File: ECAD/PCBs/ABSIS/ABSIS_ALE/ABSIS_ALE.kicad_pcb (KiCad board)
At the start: 2 copper layers, 36 x 51 mm, 16 parts, among them J1 BUS IN, J2 BUS OUT, J3 I/O #1, J4 I/O #2, J5 GND, J6 ACC PWR, U1 MAX487EESA+T

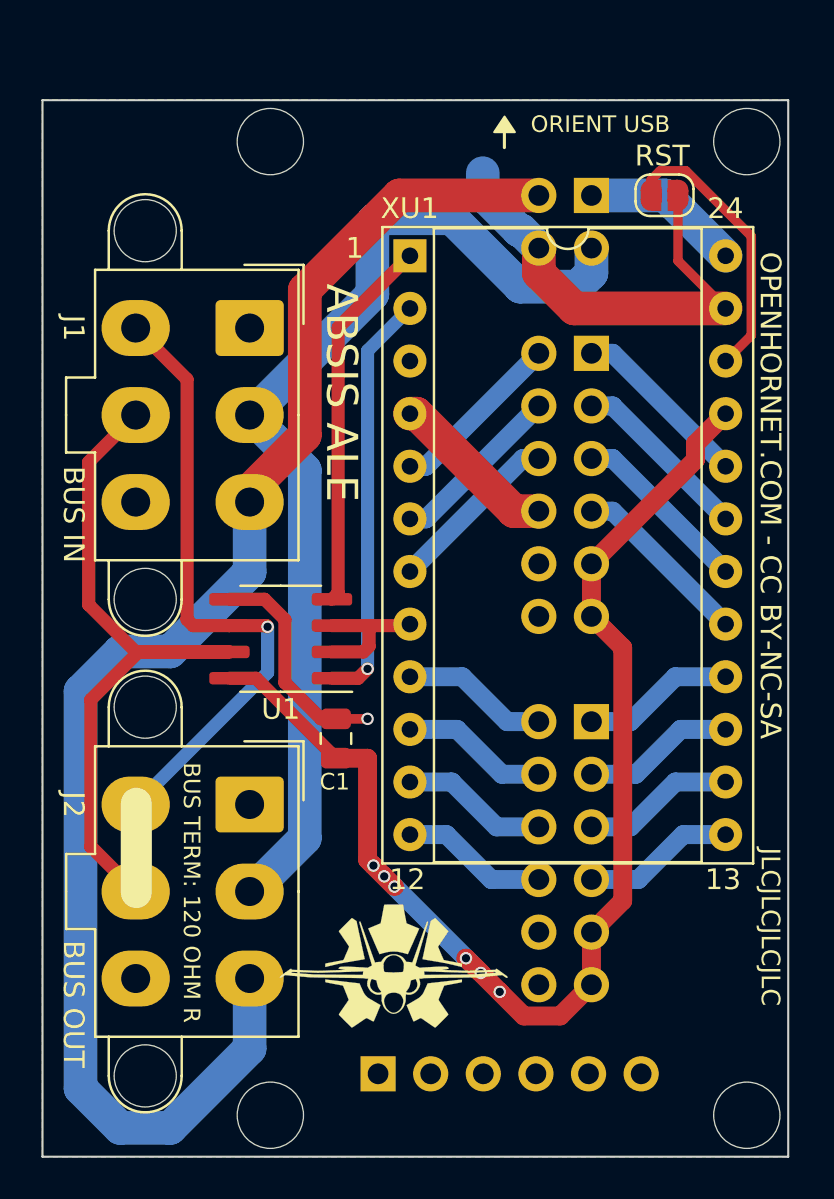
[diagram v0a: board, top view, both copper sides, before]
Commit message: OH Library Update + ABSIS_ALE Final Check
----OH_3DModels Library----
Added: PinHeader_1x06_P2.54mm_Vertical
Added: PinHeader_2x02_P2.54mm_Vertical
Added: PinHeader_2x06_P2.54mm_Vertical
Added: DIP-24_W15.24mm_Socket
Added: C_0805_2012Metric

----OH_Footprints Library----
Added: Molex_Mini-Fit_Jr_5566-06A2_2x03_P4.20mm_Vertical
Added: DIP-24_W15.24mm_Socket
Added: PinHeader_1x06_P2.54mm_Vertical
Added: PinHeader_2x02_P2.54mm_Vertical
Added: PinHeader_2x06_P2.54mm_Vertical
Added: C_0805_2012Metric
Added: SolderJumper-2_P1.3mm_Open_RoundedPad1.0x1.5mm
Added: SOIC-8_3.9x4.9mm_P1.27mm

- Updated ABSIS_ALE PCB with New footprint/Model locations
- Added 4x 3D pictures to Fold (TOP, TOP-ISO, BOT, BOT-ISO)
- Updated STEP File with 3d Models
- Regenerated Manufacturing Files with Updated Part Numbers
- Updated Schematic with correct footprint and model paths.
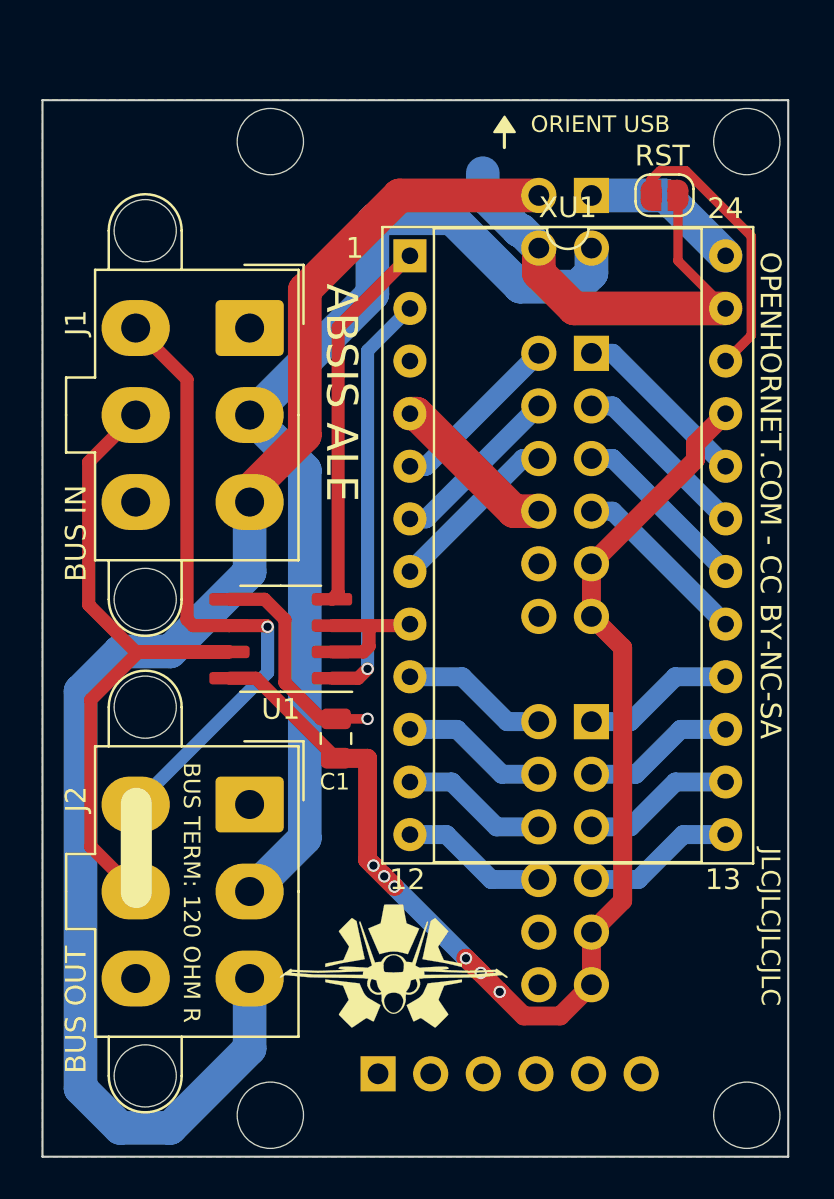
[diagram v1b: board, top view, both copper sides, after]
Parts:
- C1: footprint Capacitor_SMD:C_0805_2012Metric -> OH_Footprints:C_0805_2012Metric
- J1, J2: footprint Connector_Molex:Molex_Mini-Fit_Jr_5566-06A2_2x03_P4.20mm_Vertical -> OH_Footprints:Molex_Mini-Fit_Jr_5566-06A2_2x03_P4.20mm_Vertical
- J3, J4: footprint Connector_PinHeader_2.54mm:PinHeader_2x06_P2.54mm_Vertical -> OH_Footprints:PinHeader_2x06_P2.54mm_Vertical
- J5: footprint Connector_PinHeader_2.54mm:PinHeader_1x06_P2.54mm_Vertical -> OH_Footprints:PinHeader_1x06_P2.54mm_Vertical
- J6: footprint Connector_PinHeader_2.54mm:PinHeader_2x02_P2.54mm_Vertical -> OH_Footprints:PinHeader_2x02_P2.54mm_Vertical
- XU1: footprint Package_DIP:DIP-24_W15.24mm_Socket -> OH_Footprints:DIP-24_W15.24mm_Socket

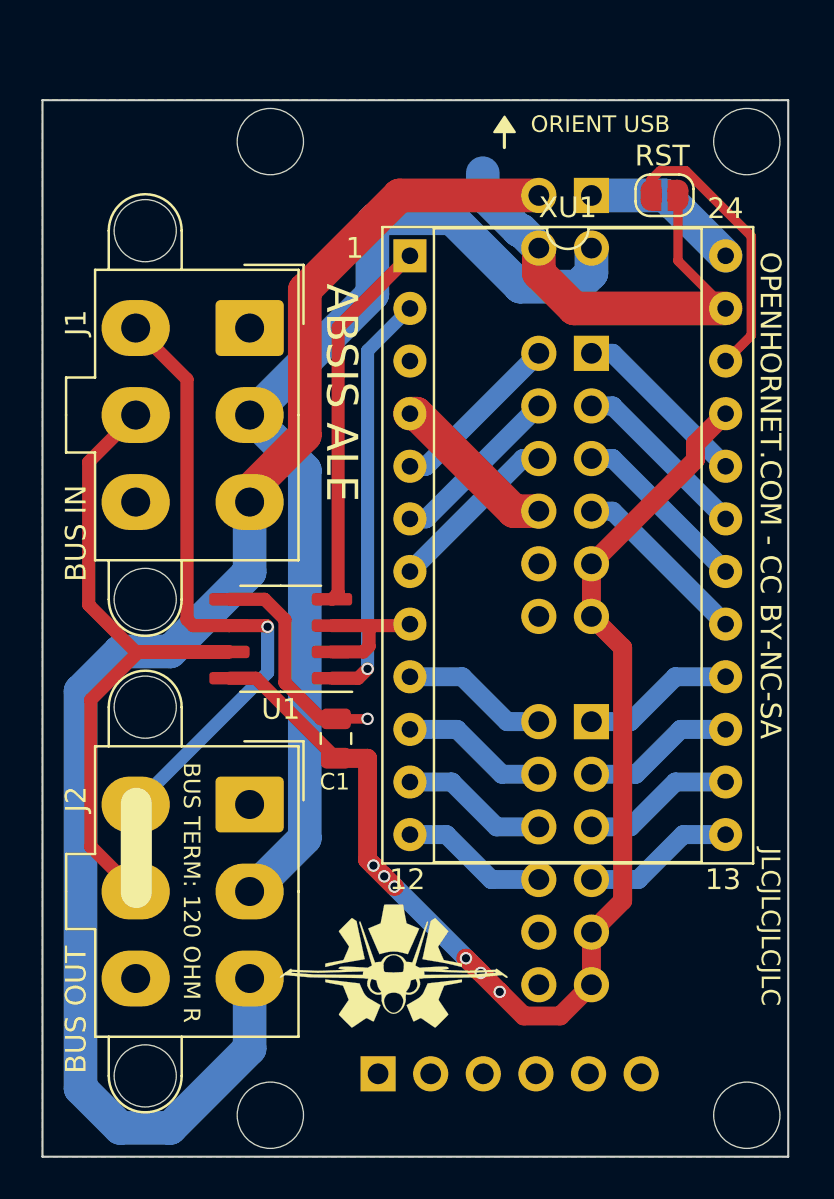
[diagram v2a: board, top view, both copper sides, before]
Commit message: Removed excess Backlight_controller.STEP
No idea why ABSIS_Backlight Controller.STEP was in every MCAD folder for PCBs.  Might have been a glitch, but they were all time stamped the same so I know I didn't manually move them in there.  Took them all out.
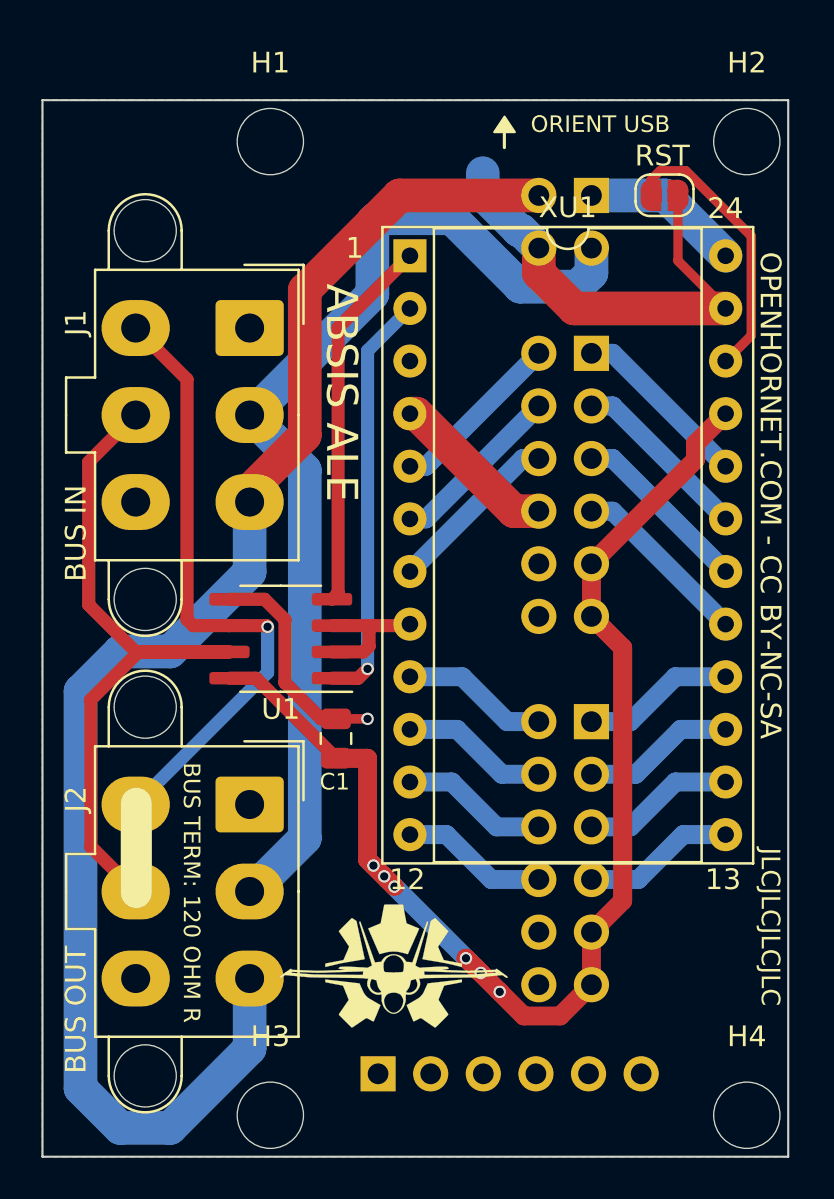
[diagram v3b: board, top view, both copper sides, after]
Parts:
- H1, H2, H3, H4: footprint MountingHole:MountingHole_3.2mm_M3_DIN965 -> OH_Footprints:MountingHole_3.2mm_M3_DIN965
- LOGO1, LOGO2: footprint KiCAD Libraries:OH_LOGO_ONLY_11x6mm -> OH_Footprints:OH_LOGO_ONLY_11x6mm
- RST1: footprint Jumper:SolderJumper-2_P1.3mm_Open_RoundedPad1.0x1.5mm -> OH_Footprints:SolderJumper-2_P1.3mm_Open_RoundedPad1.0x1.5mm
- U1: footprint Package_SO:SOIC-8_3.9x4.9mm_P1.27mm -> OH_Footprints:SOIC-8_3.9x4.9mm_P1.27mm

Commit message: Review:  ABSIS_ALE 100% Complete.
ABSIS_ALE (Revision 2) 100% Complete.
Fixed Silkscreen
Updated Manufacturing Files to reflect changes
Added Pin Header models and footprints to Libraries
Updated PCB Footprints to point to OH Libraries
STEP Model updated to reflect changes.
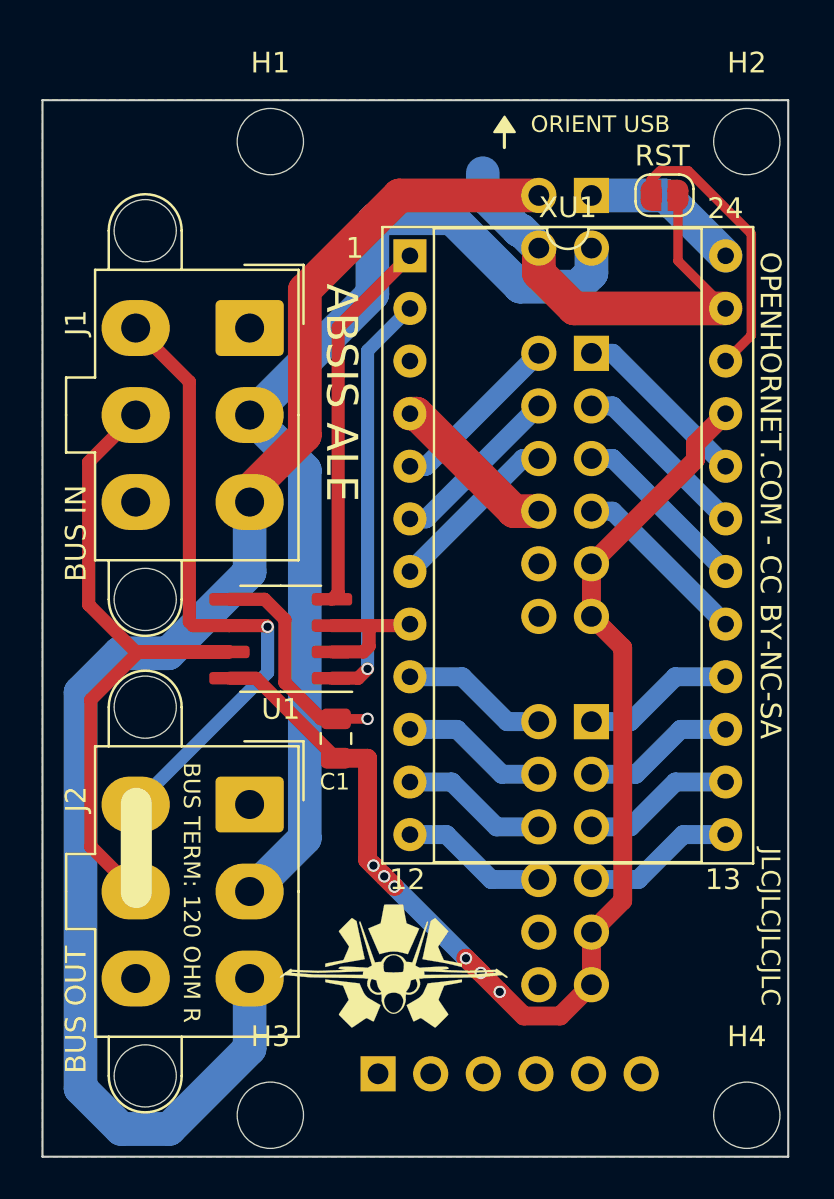
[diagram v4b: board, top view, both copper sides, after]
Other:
- board text added: "+12V"
- board text added: "+3.3V"
- board text added: "D4/A6"
- board text added: "D8/A8"
- board text added: "OPENHORNET.COM - CC BY-NC-SA - REV: 2"
- board text added: "~{D10/A10}"
- board text added: "~{D6/A7}"
- board text added: "~{D9/A9}"
- board text removed: "12V"
- board text removed: "3.3"
- board text removed: "D4/ A6"
- board text removed: "OPENHORNET.COM - CC BY-NC-SA - REV: 1"
- board text removed: "~{10/ A10}"
- board text removed: "~{D6/ A7}"
- board text removed: "~{D8/ A8}"
- board text removed: "~{D9/ A9}"

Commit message: SELECT JETT Panel STEP updated for F360
Updated Hall Sensor silkscreen to prevent confusion on Diode placement.  Updated images
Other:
- board text added: "12V"
- board text added: "3.3V"
- board text removed: "+12V"
- board text removed: "+3.3V"
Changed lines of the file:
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@@
     (effects (font (size 0.8 0.8) (thickness 0.15)) (justify mirror))
   )
-  (gr_text "+3.3V" (at 142.1808 68.2264) (layer "B.SilkS")
+  (gr_text "3.3V" (at 142.511 68.2772) (layer "B.SilkS")
     (effects (font (size 0.8 0.8) (thickness 0.15)) (justify mirror))
   )
@@
     (effects (font (size 0.8 0.8) (thickness 0.15)) (justify mirror))
   )
-  (gr_text "+12V" (at 151.9852 68.4296) (layer "B.SilkS")
+  (gr_text "12V" (at 151.4264 68.455) (layer "B.SilkS")
     (effects (font (size 0.8 0.8) (thickness 0.15)) (justify mirror))
   )

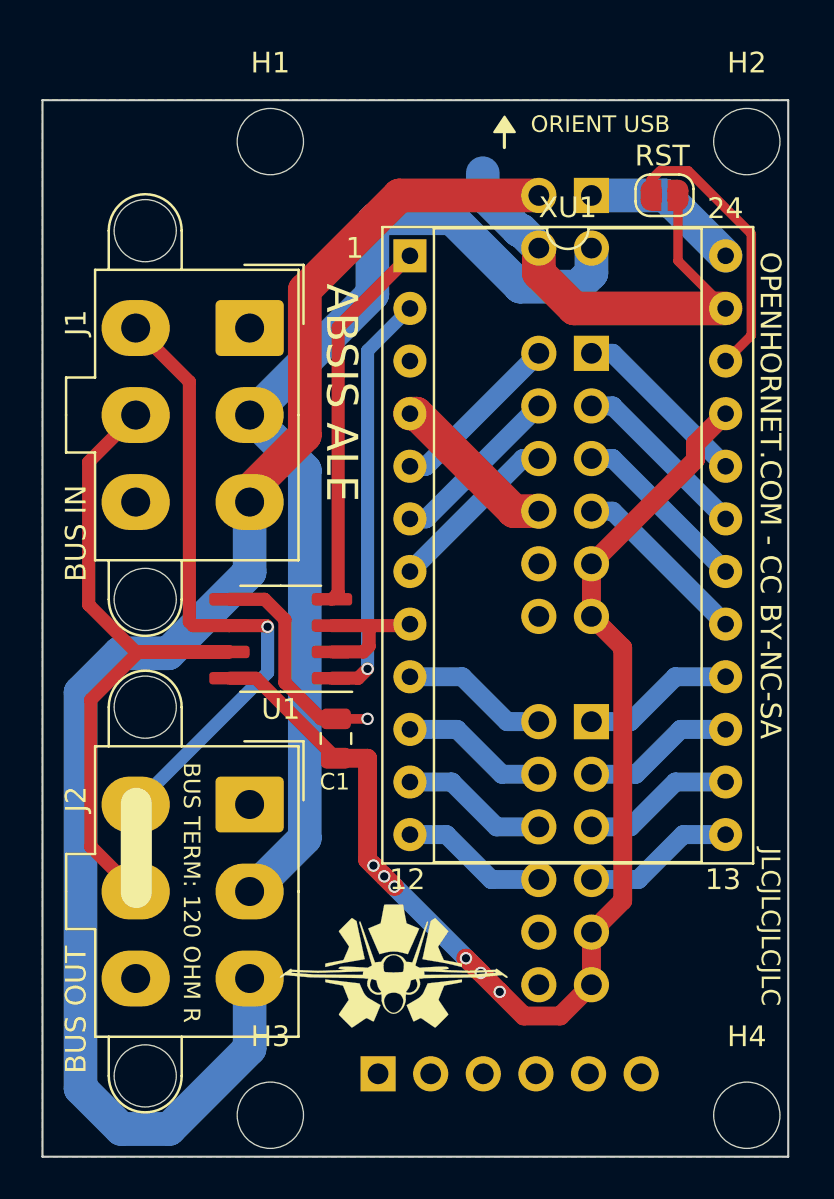
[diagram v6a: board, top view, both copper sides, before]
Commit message: KiCad 7 Transition - ABSIS_ALE
KiCad 7 Transition - ABSIS_ALE

Schematic standardization:
1;  Updated schematic notes
2:  Updated symbol links
3:  Recompiled Assets and Manufacturing Files

Added ABSIS symbols to OH_library
Reset Jumper
Pro Micro
Molex 2x3 connectors for Bus
Pin Headers
RS485 Bus Controller
Pro Micro

**Edited COMM Panel schematic - switched location of TP 2 & 3
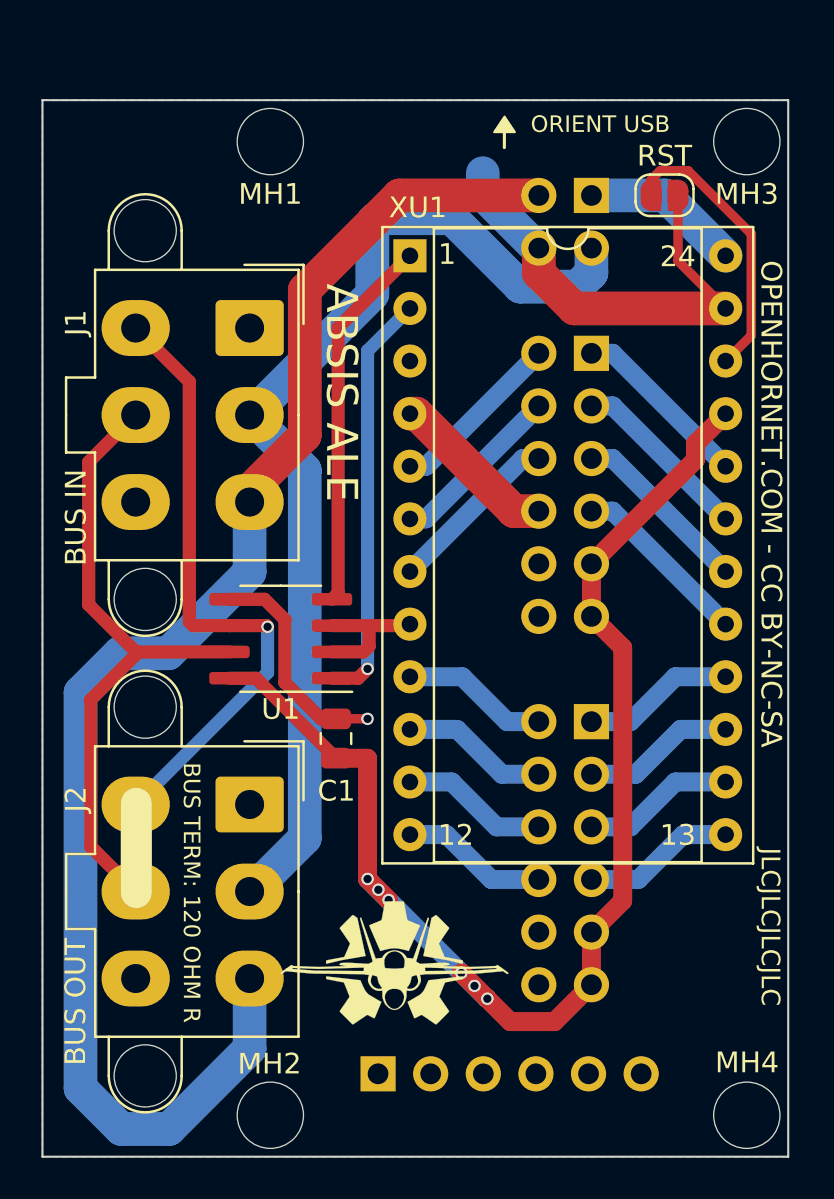
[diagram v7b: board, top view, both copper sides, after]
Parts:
- J1: value BUS IN -> Mini-Fit Jr. 2x03
- J2: value BUS OUT -> Mini-Fit Jr. 2x03
- J3: value I/O #1 -> PinHeader_2x06
- J4: value I/O #2 -> PinHeader_2x06
- J5: value GND -> PinHeader_1x06
- J6: value ACC PWR -> PinHeader_2x02
- LOGO1, LOGO2: value OpenHornetLogoSmall -> LOGO; footprint OH_Footprints:OH_LOGO_ONLY_11x6mm -> OH_Footprints:LOGO_OH_NoText_Small
- MH1: renamed from H1; value MH -> M3 / 3.2mm
- MH2: renamed from H3; value MH -> M3 / 3.2mm
- MH3: renamed from H2; value MH -> M3 / 3.2mm
- MH4: renamed from H4; value MH -> M3 / 3.2mm
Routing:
- net /BUS-B: track 35.6 -> 31.3 mm
- net +5V: track 60.7 -> 63.2 mm
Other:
- board text added: "A6"
- board text added: "A8"
- board text added: "D4"
- board text added: "D8"
- board text added: "~{A10}"
- board text added: "~{A7}"
- board text added: "~{A9}"
- board text added: "~{D10}"
- board text added: "~{D6}"
- board text added: "~{D9}"
- board text removed: "D4/A6"
- board text removed: "D8/A8"
- board text removed: "~{D10/A10}"
- board text removed: "~{D6/A7}"
- board text removed: "~{D9/A9}"

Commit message: Updated ABSIS ALE power circuit.
- Added 1N5819WS (D1) between 12V SUPPLY and RAW pin of Pro-Micro.
- Incremented to Rev 3.
- Added better verbiage on PCB of how to terminate RS485 bus.
- Added note to schematic to remove F1/ensure JP1 is not soldered on Pro-Micro if external power is applied.

Closes #991
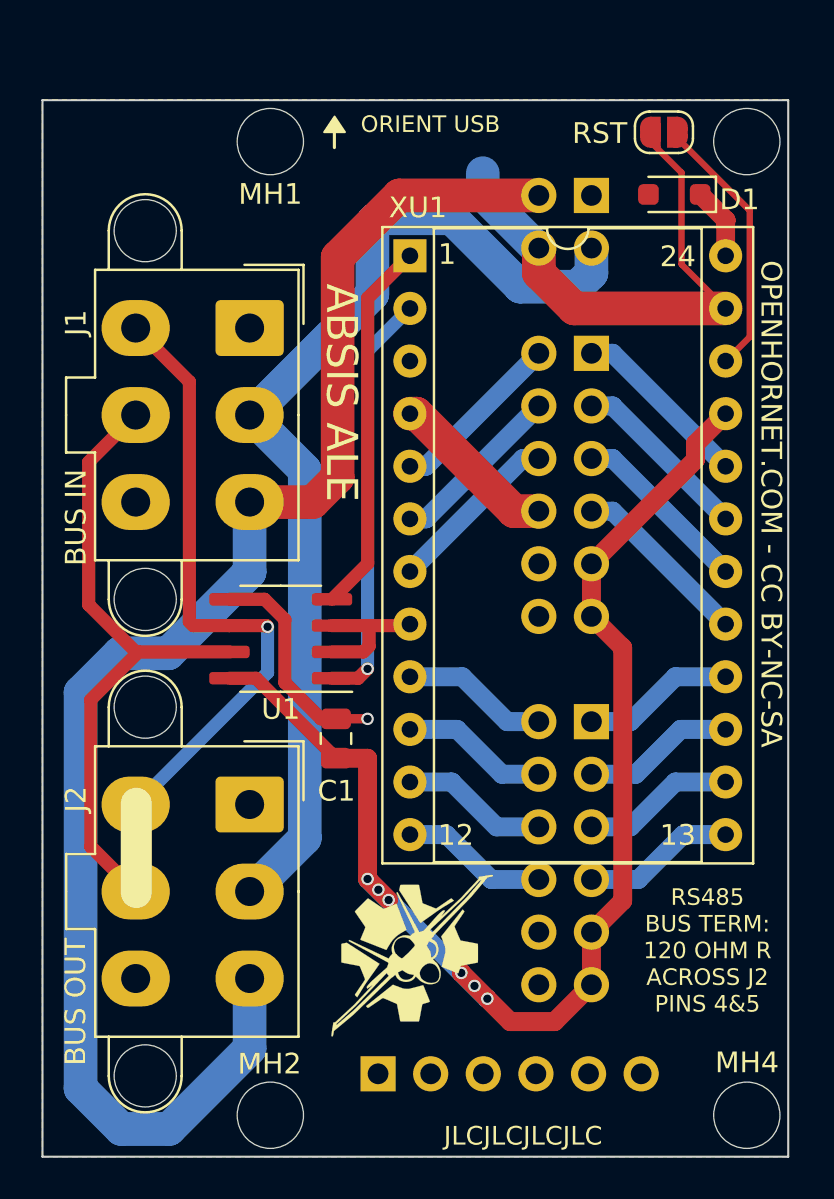
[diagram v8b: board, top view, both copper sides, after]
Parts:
- added D1: 1N5819WS, Diode_SMD:D_SOD-323_HandSoldering, F.Cu at (152.3, 68.4)
- moved RST1 3.04 mm to (151.8, 65.4), turned to 0 degrees
- moved LOGO2 1.05 mm to (139.5, 105.0), turned to 45 degrees
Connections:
- XU1 pad 24: /+12V_SUPPLY -> Net-(D1-K)
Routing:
- net /+12V_SUPPLY: track 7.68 -> 0.00 mm
- net GND: track 41.1 -> 44.7 mm
- net Net-(D1-K): track 0.00 -> 3.49 mm
- net /+3.3V_SUPPLY: track 71.5 -> 73.3 mm
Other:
- board text added: "OPENHORNET.COM - CC BY-NC-SA - REV: 3"
- board text added: "RS485 BUS TERM: 120 OHM R ACROSS J2 PINS 4&5"
- board text removed: "BUS TERM: 120 OHM R"
- board text removed: "OPENHORNET.COM - CC BY-NC-SA - REV: 2"
